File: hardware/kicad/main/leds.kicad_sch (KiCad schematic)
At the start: 103 parts, among them U43 SN74LV1T34DBVR

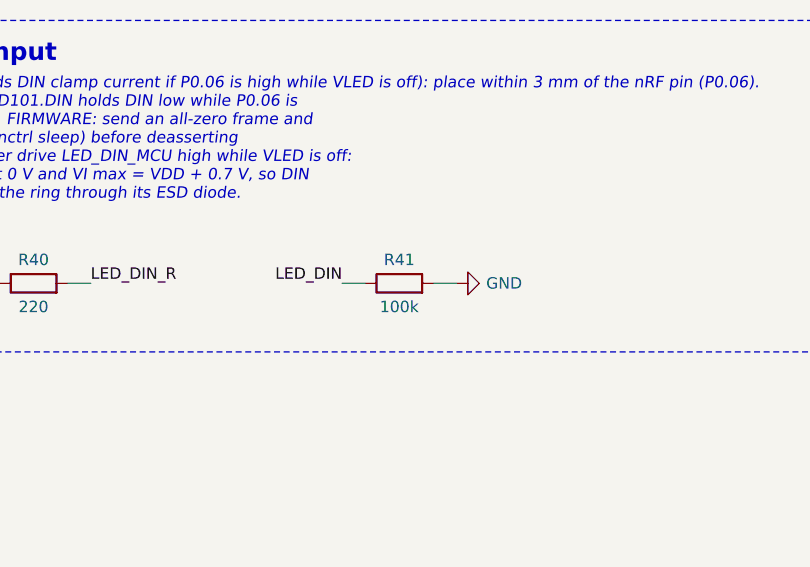
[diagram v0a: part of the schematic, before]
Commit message: Apply schematic review fixes; base board routes to 100% with zero DRC errors
- OLED VCC input disconnect is now a TPS22917 load switch (CT to VIN) instead
  of an AO3401A/2N7002 with no real inrush control
- TPD4E05U06 TVS on the TMAG5273 lines (floating 316L ring passes 2.4 mm away)
- piezo: 470R series + 1M bleed; LED_DIN pull-down moved to the shifter input
- base: explicit 2x4 DSBGA fan-out for the BQ25180, 0.4 mm power tracks,
  BAT+/GND silkscreen at the battery connector, JEITA NTC over the pack
- SPEC: side-entry link headers on both boards, 28 AWG power leads

Co-Authored-By: Claude Opus 5.5 <noreply@anthropic.com>
Claude-Session: https://claude.ai/code/session_01P3cqdBhxLcWY3sGUVf9LAJ
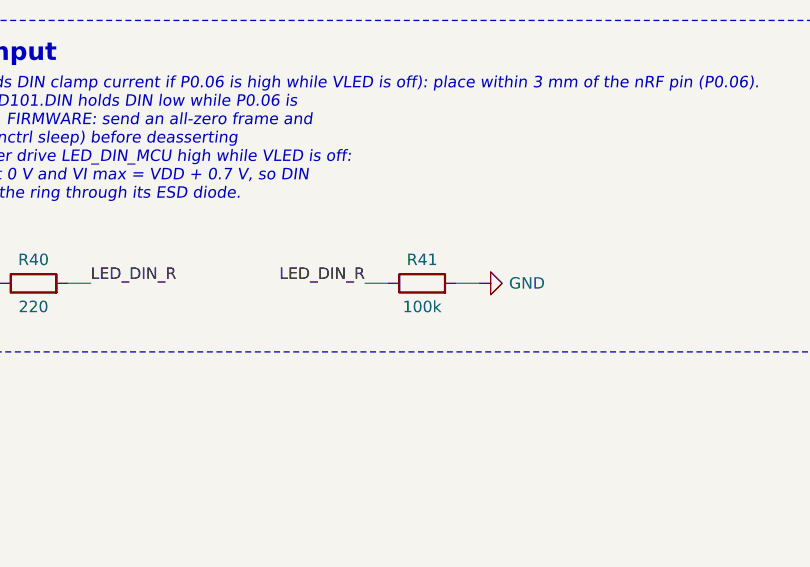
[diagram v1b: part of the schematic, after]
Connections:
- net LED_DIN: no longer R41.1
- net LED_DIN_R: now also R41.1
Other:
- moved on the sheet: R41
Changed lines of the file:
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@@
 	(symbol
 		(lib_id "Device:R")
-		(at 76.2 63.5 90)
+		(at 78.74 63.5 90)
 		(unit 1)
 		(exclude_from_sim no)
@@
 		(dnp no)
 		(property "Reference" "R41"
-			(at 76.2 60.884 90)
+			(at 78.74 60.884 90)
 			(effects
 				(font
@@
 		)
 		(property "Value" "100k"
-			(at 76.2 66.116 90)
+			(at 78.74 66.116 90)
 			(effects
 				(font
@@
 		)
 		(property "Footprint" "Resistor_SMD:R_0402_1005Metric"
-			(at 76.2 63.5 0)
+			(at 78.74 63.5 0)
 			(effects
 				(font
@@
 		)
 		(property "Datasheet" "~"
-			(at 76.2 63.5 0)
+			(at 78.74 63.5 0)
 			(effects
 				(font
@@
 		)
 		(property "Description" "Resistor"
-			(at 76.2 63.5 0)
+			(at 78.74 63.5 0)
 			(effects
 				(font
@@
 		)
 		(property "MPN" "0402WGF1003TCE"
-			(at 76.2 63.5 0)
+			(at 78.74 63.5 0)
 			(effects
 				(font
@@
 		)
 		(property "Manufacturer" "UNI-ROYAL"
-			(at 76.2 63.5 0)
+			(at 78.74 63.5 0)
 			(effects
 				(font
@@
 		)
 		(property "LCSC" "C25741"
-			(at 76.2 63.5 0)
+			(at 78.74 63.5 0)
 			(effects
 				(font
@@
 	)
 	(wire
-		(pts (xy 72.39 63.5) (xy 69.85 63.5))
+		(pts (xy 74.93 63.5) (xy 72.39 63.5))
 		(stroke
 			(width 0)
@@
 		)
 	)
-	(label "LED_DIN"
-		(at 69.85 63.5 180)
+	(label "LED_DIN_R"
+		(at 72.39 63.5 180)
 		(effects
 			(font
@@
 	)
 	(wire
-		(pts (xy 80.01 63.5) (xy 82.55 63.5))
+		(pts (xy 82.55 63.5) (xy 85.09 63.5))
 		(stroke
 			(width 0)
@@
 	(symbol
 		(lib_id "power:GND")
-		(at 82.55 63.5 90)
+		(at 85.09 63.5 90)
 		(unit 1)
 		(exclude_from_sim no)
@@
 		(dnp no)
 		(property "Reference" "#PWR05001"
-			(at 82.55 63.5 0)
+			(at 85.09 63.5 0)
 			(effects
 				(font
@@
 		)
 		(property "Value" "GND"
-			(at 85.85 63.5 90)
+			(at 88.39 63.5 90)
 			(effects
 				(font
@@
 		)
 		(property "Footprint" ""
-			(at 82.55 63.5 0)
+			(at 85.09 63.5 0)
 			(effects
 				(font
@@
 		)
 		(property "Datasheet" ""
-			(at 82.55 63.5 0)
+			(at 85.09 63.5 0)
 			(effects
 				(font
@@
 		)
 		(property "Description" ""
-			(at 82.55 63.5 0)
+			(at 85.09 63.5 0)
 			(effects
 				(font

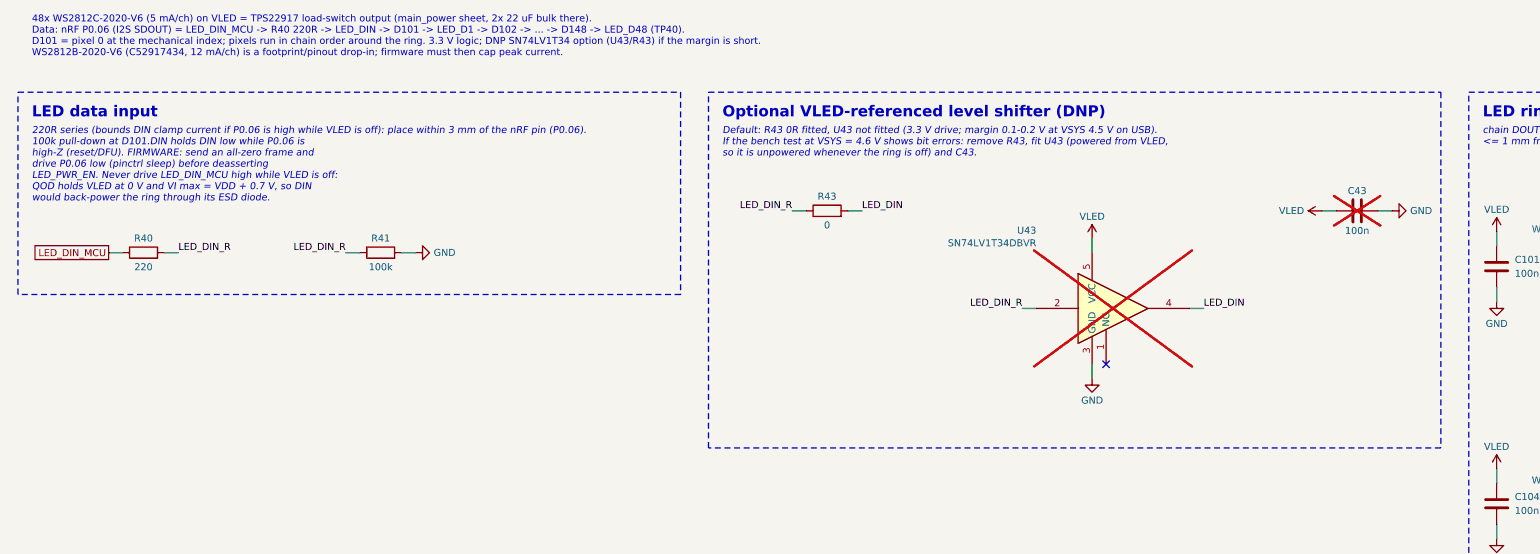
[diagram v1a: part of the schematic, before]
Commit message: Schematic notes: J1 at r 19.5, VLED fall 24/26.6 ms, hot-plug 4.49-5.49 V, SM04B J2, 100k press pull-down, SYS_REG 4.4 V, side-entry J3, LED data path and margins
Notes only; netlists unchanged. Base board still DRC-clean with schematic parity.

Co-Authored-By: Claude Opus 5.5 <noreply@anthropic.com>
Claude-Session: https://claude.ai/code/session_01P3cqdBhxLcWY3sGUVf9LAJ
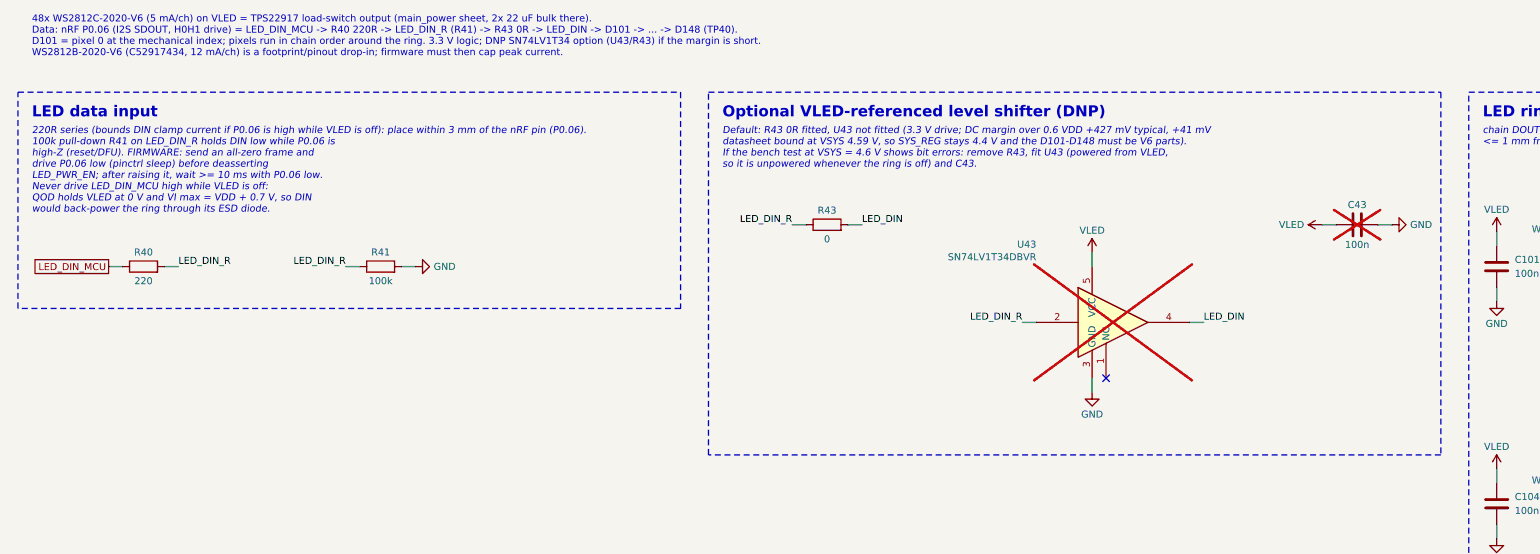
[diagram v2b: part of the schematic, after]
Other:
- note added: "220R series (bounds DIN clamp current if P0.06 is high while VLED is off): place within 3 mm of the nRF pin (P0.06). 100k pull-down R41 on LED_DIN_R holds DIN low while P0.06 is high-Z (reset/DFU). FIRMWARE: send an all-zero frame and drive P0.06 low (pinctrl sleep) before deasserting LED_PWR_EN; after raising it, wait >= 10 ms with P0.06 low. Never drive LED_DIN_MCU high while VLED is off: QOD h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"
- note added: "48x WS2812C-2020-V6 (5 mA/ch) on VLED = TPS22917 load-switch output (main_power sheet, 2x 22 uF bulk there). Data: nRF P0.06 (I2S SDOUT, H0H1 drive) = LED_DIN_MCU -> R40 220R -> LED_DIN_R (R41) -> R43 0R -> LED_DIN -> D101 -> ... -> D148 (TP40). D101 = pixel 0 at the mechanical index; pixels run in chain order around the ring. 3.3 V logic; DNP SN74LV1T34 option (U43/R43) if the margin is short. W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"
- note added: "Default: R43 0R fitted, U43 not fitted (3.3 V drive; DC margin over 0.6 VDD +427 mV typical, +41 mV datasheet bound at VSYS 4.59 V, so SYS_REG stays 4.4 V and the D101-D148 must be V6 parts). If the bench test at VSYS = 4.6 V shows bit errors: remove R43, fit U43 (powered from VLED, so it is unpowered whenever the ring is off) and C43."
- note removed: "220R series (bounds DIN clamp current if P0.06 is high while VLED is off): place within 3 mm of the nRF pin (P0.06). 100k pull-down at D101.DIN holds DIN low while P0.06 is high-Z (reset/DFU). FIRMWARE: send an all-zero frame and drive P0.06 low (pinctrl sleep) before deasserting LED_PWR_EN. Never drive LED_DIN_MCU high while VLED is off: QOD holds VLED at 0 V and VI max = VDD + 0.7 V, so DIN wou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"
- note removed: "48x WS2812C-2020-V6 (5 mA/ch) on VLED = TPS22917 load-switch output (main_power sheet, 2x 22 uF bulk there). Data: nRF P0.06 (I2S SDOUT) = LED_DIN_MCU -> R40 220R -> LED_DIN -> D101 -> LED_D1 -> D102 -> ... -> D148 -> LED_D48 (TP40). D101 = pixel 0 at the mechanical index; pixels run in chain order around the ring. 3.3 V logic; DNP SN74LV1T34 option (U43/R43) if the margin is short. WS2812B-2020-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"
- note removed: "Default: R43 0R fitted, U43 not fitted (3.3 V drive; margin 0.1-0.2 V at VSYS 4.5 V on USB). If the bench test at VSYS = 4.6 V shows bit errors: remove R43, fit U43 (powered from VLED, so it is unpowered whenever the ring is off) and C43."
- moved on the sheet: C43, R40, R41, R43, U43
